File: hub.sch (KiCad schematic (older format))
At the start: 22 parts

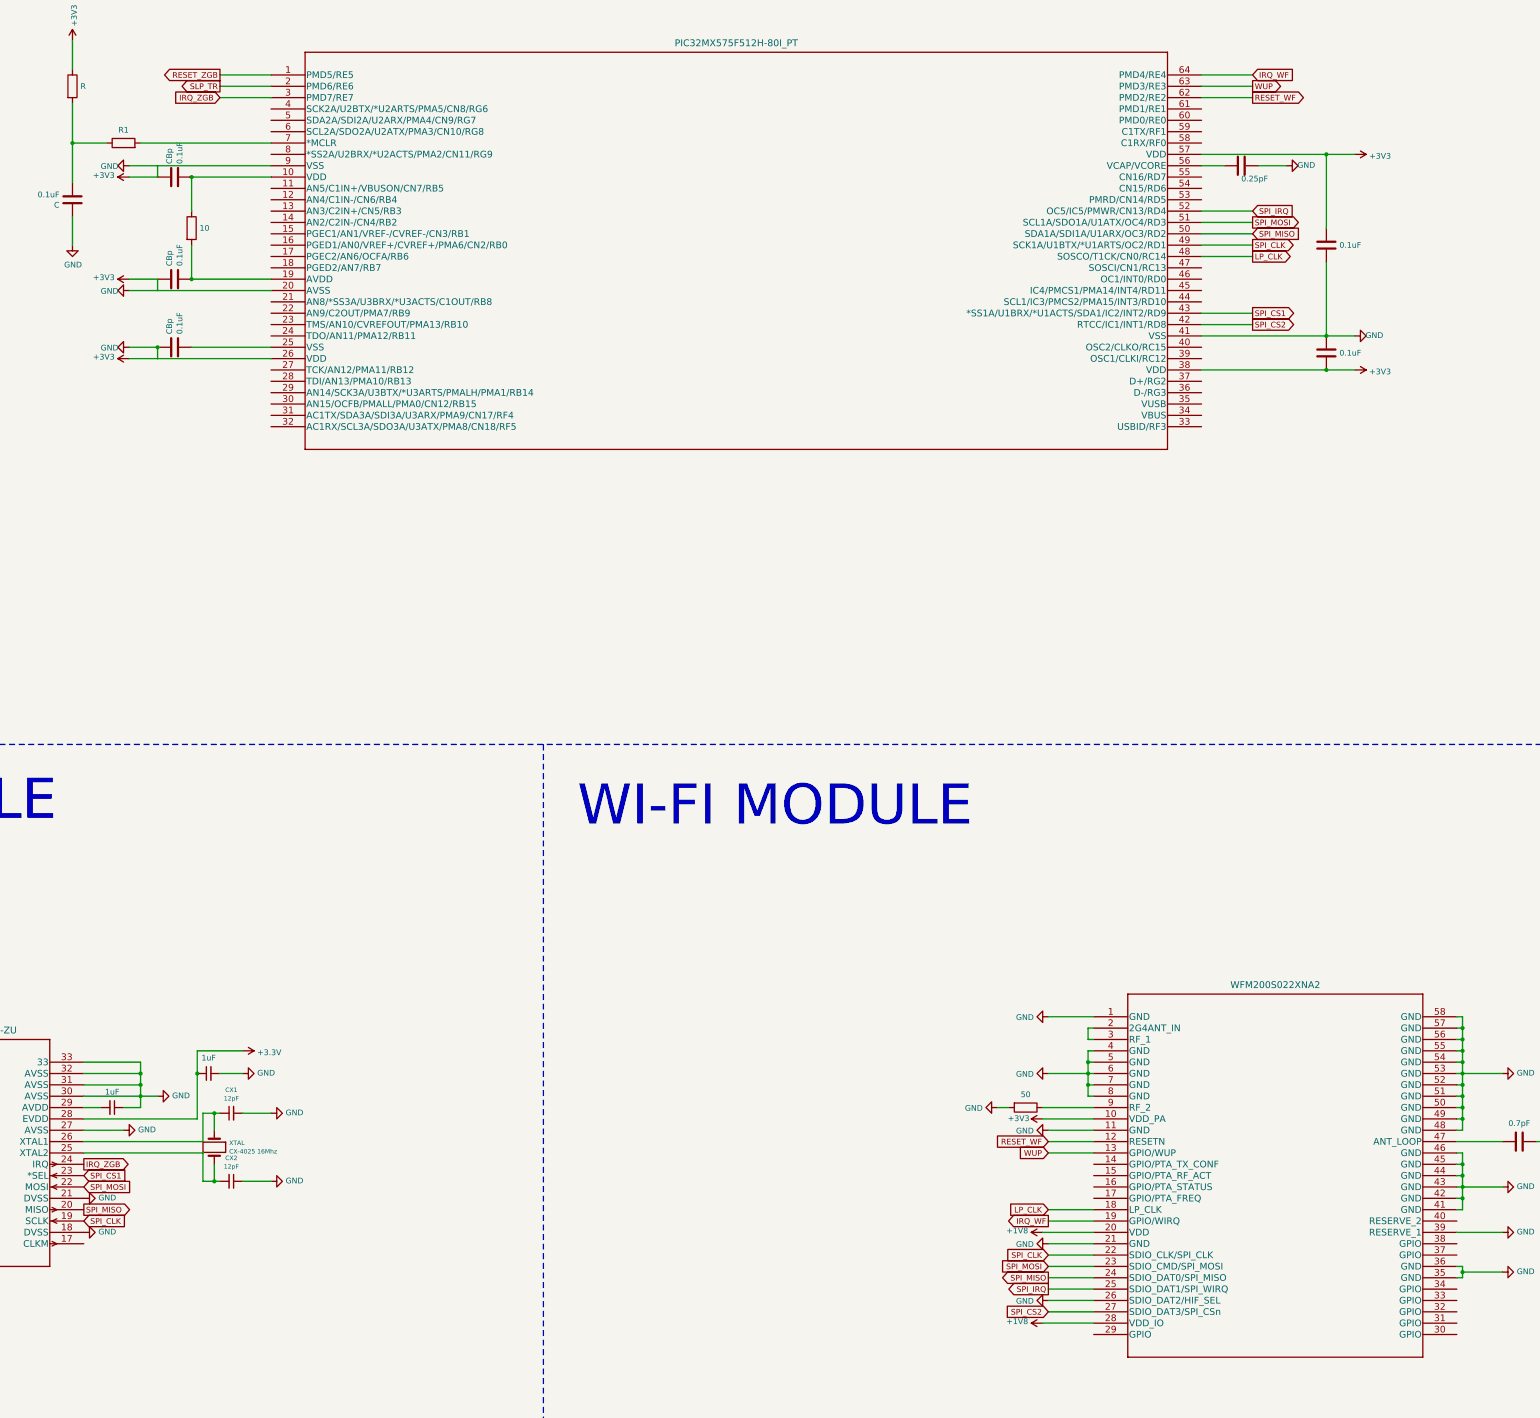
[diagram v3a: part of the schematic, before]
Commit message: Add cube PCB design
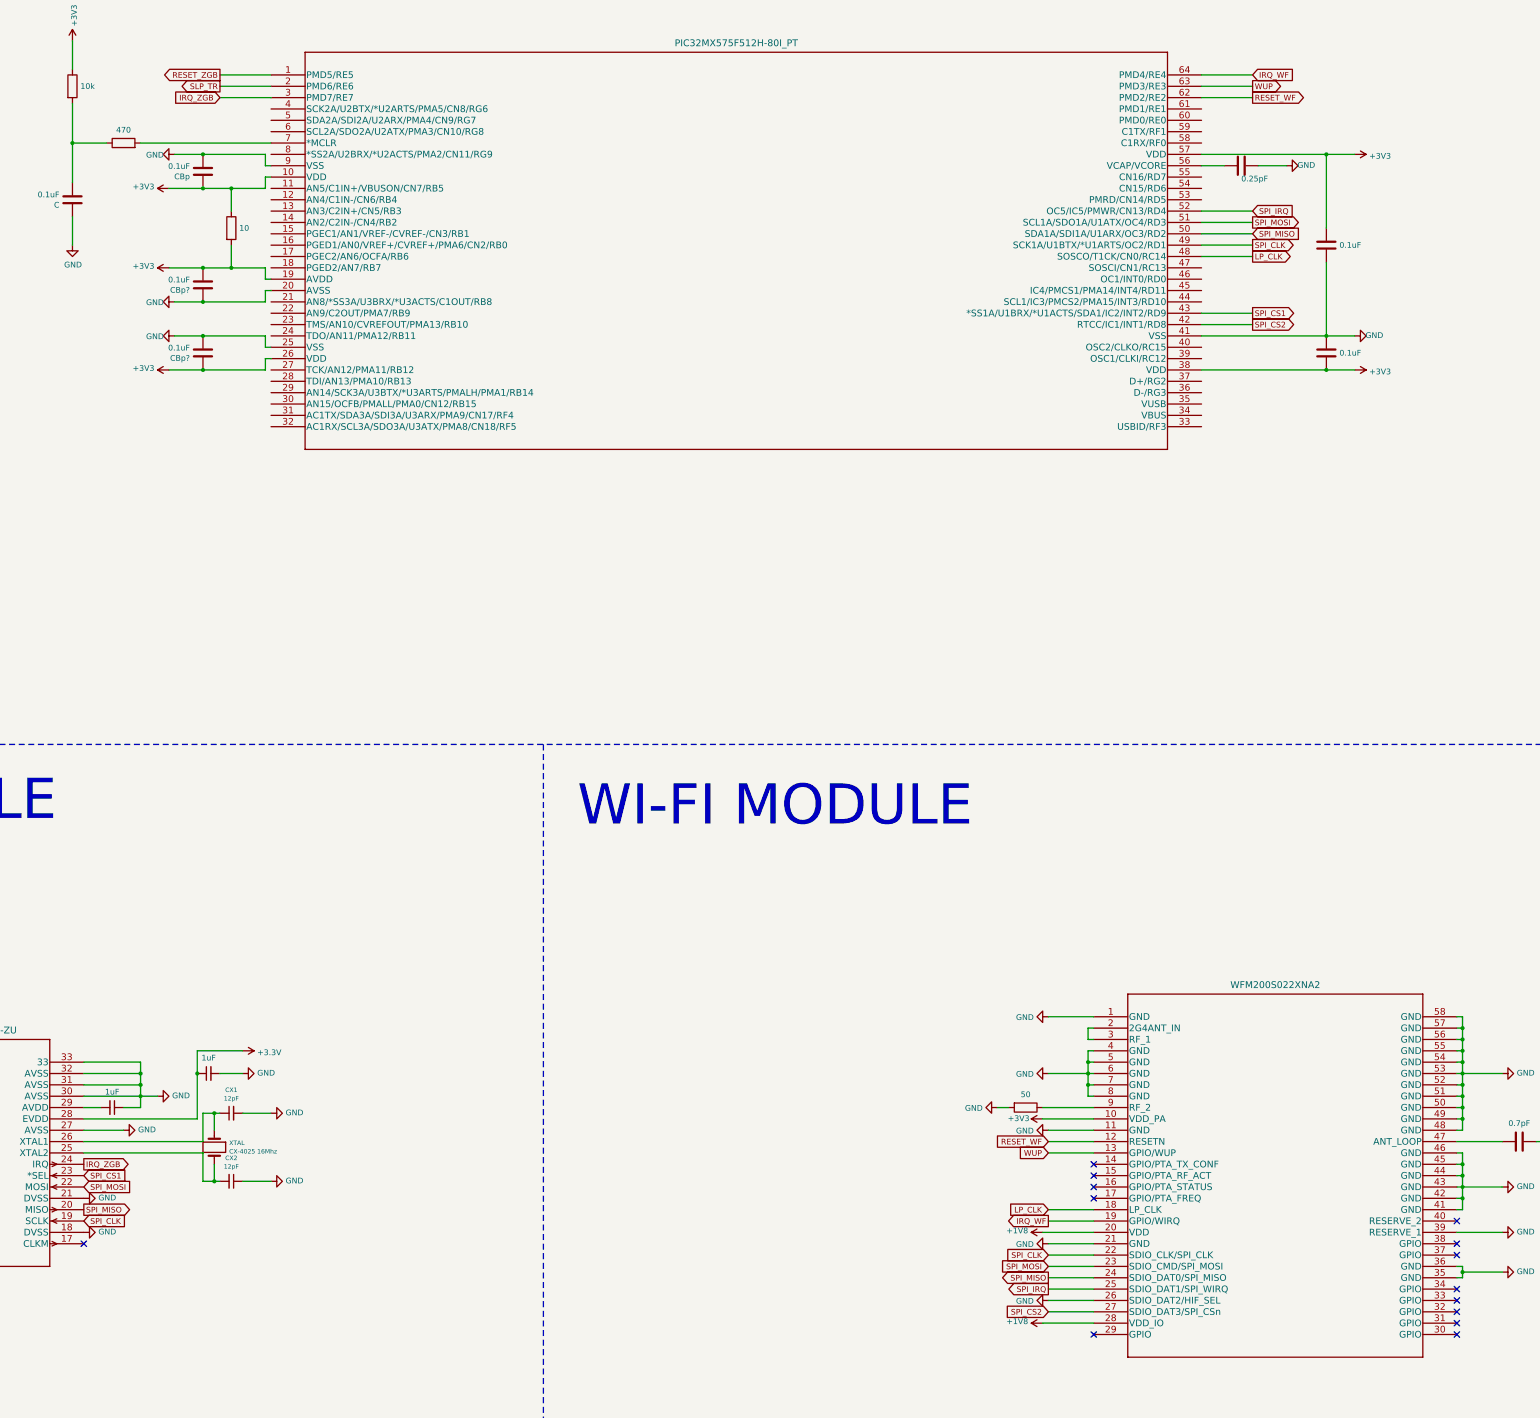
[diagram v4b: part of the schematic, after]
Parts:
- removed CBp (x2): 0.1uF, symbol Device:C
- removed R?: 10, symbol Device:R
- added CBp? (x2): 0.1uF, symbol Device:C
- added r: 10, symbol Device:R
- R?: value R -> 10k
- R?: value R1 -> 470
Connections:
- net +3V3: now also U?.10 (VDD), U?.19 (AVDD), CBp?.1, CBp?.2, r.1, r.2; no longer C.1, C?.1, C?.1, C?.1, C?.2, CB?.1, CB?.2, CB?.2, CX1.2, CX2.1, R?.2, U?.1 (DIG3), U?.10 (DIG2), U?.12 (DVSS), U?.16 (DVSS), U?.18 (DVSS), U?.2 (DIG4), U?.20 (AVSS), U?.21 (DVSS), U?.27 (AVSS), U?.3 (AVSS), U?.30 (AVSS), U?.31 (AVSS), U?.32 (AVSS), U?.33, U?.41 (VSS), U?.6 (AVSS), U?.7 (DVSS), U?.9 (DIG1), U?.9 (VSS), WiFi.1 (GND), WiFi.11 (GND), WiFi.21 (GND), WiFi.26 (SDIO_DAT2/HIF_SEL), WiFi.35 (GND), WiFi.36 (GND), WiFi.39 (RESERVE_1), WiFi.4 (GND), WiFi.41 (GND), WiFi.42 (GND), WiFi.43 (GND), WiFi.44 (GND), WiFi.45 (GND), WiFi.46 (GND), WiFi.48 (GND), WiFi.49 (GND), WiFi.5 (GND), WiFi.50 (GND), WiFi.51 (GND), WiFi.52 (GND), WiFi.53 (GND), WiFi.54 (GND), WiFi.55 (GND), WiFi.56 (GND), WiFi.57 (GND), WiFi.58 (GND), WiFi.6 (GND), WiFi.7 (GND), WiFi.8 (GND), cb.2
- net GND: now reaches CBp.2
- net GND: now also C.1, C?.1, C?.1, C?.1, C?.2, CB?.1, CB?.2, CB?.2, CX1.2, CX2.1, R?.2, U?.1 (DIG3), U?.10 (DIG2), U?.12 (DVSS), U?.16 (DVSS), U?.18 (DVSS), U?.2 (DIG4), U?.20 (AVSS), U?.21 (DVSS), U?.25 (VSS), U?.27 (AVSS), U?.3 (AVSS), U?.30 (AVSS), U?.31 (AVSS), U?.32 (AVSS), U?.33, U?.41 (VSS), U?.6 (AVSS), U?.7 (DVSS), U?.9 (DIG1), U?.9 (VSS), WiFi.1 (GND), WiFi.11 (GND), WiFi.21 (GND), WiFi.26 (SDIO_DAT2/HIF_SEL), WiFi.35 (GND), WiFi.36 (GND), WiFi.39 (RESERVE_1), WiFi.4 (GND), WiFi.41 (GND), WiFi.42 (GND), WiFi.43 (GND), WiFi.44 (GND), WiFi.45 (GND), WiFi.46 (GND), WiFi.48 (GND), WiFi.49 (GND), WiFi.5 (GND), WiFi.50 (GND), WiFi.51 (GND), WiFi.52 (GND), WiFi.53 (GND), WiFi.54 (GND), WiFi.55 (GND), WiFi.56 (GND), WiFi.57 (GND), WiFi.58 (GND), WiFi.6 (GND), WiFi.7 (GND), WiFi.8 (GND), cb.2, CBp?.1, CBp?.2; no longer U?.10 (VDD)
- no-connect marks 0 -> 14
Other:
- moved on the sheet: CBp
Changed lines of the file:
@@
 L Device:C CBp
 U 1 1 609B9B76
-P 5850 3850
-F 0 "CBp" H 5965 3896 50  0000 L CNN
-F 1 "0.1uF" H 5965 3805 50  0000 L CNN
-F 2 "" H 5888 3700 50  0001 C CNN
-F 3 "~" H 5850 3850 50  0001 C CNN
-	1    5850 3850
-	0    -1   -1   0
+P 6100 3800
+F 0 "CBp" H 6215 3846 50  0000 L CNN
+F 1 "0.1uF" H 6215 3755 50  0000 L CNN
+F 2 "" H 6138 3650 50  0001 C CNN
+F 3 "~" H 6100 3800 50  0001 C CNN
+	1    6100 3800
+	-1   0    0    1
 $EndComp
 $Comp
@@
 Wire Wire Line
 	14900 5550 16000 5550
-Wire Wire Line
-	5700 3750 5700 3850
-Wire Wire Line
-	6700 5350 6000 5350
-$Comp
-L Device:C CBp
-U 1 1 60AF944E
-P 5850 5350
-F 0 "CBp" H 5965 5396 50  0000 L CNN
-F 1 "0.1uF" H 5965 5305 50  0000 L CNN
-F 2 "" H 5888 5200 50  0001 C CNN
-F 3 "~" H 5850 5350 50  0001 C CNN
-	1    5850 5350
-	0    -1   -1   0
-$EndComp
-Wire Wire Line
-	5700 5350 5700 5450
-Wire Wire Line
-	5700 5450 6700 5450
-Wire Wire Line
-	6700 4750 6000 4750
-$Comp
-L Device:C CBp
-U 1 1 60B009EA
-P 5850 4750
-F 0 "CBp" H 5965 4796 50  0000 L CNN
-F 1 "0.1uF" H 5965 4705 50  0000 L CNN
-F 2 "" H 5888 4600 50  0001 C CNN
-F 3 "~" H 5850 4750 50  0001 C CNN
-	1    5850 4750
-	0    -1   -1   0
-$EndComp
-Wire Wire Line
-	5700 4750 5700 4850
-Wire Wire Line
-	5700 4850 6700 4850
-Wire Wire Line
-	6000 3850 6700 3850
-Wire Wire Line
-	5700 3750 6700 3750
-Wire Wire Line
-	6000 3850 6000 4150
-Connection ~ 6000 3850
-Connection ~ 6000 4750
-$Comp
-L Device:R R?
-U 1 1 60B1E6B4
-P 6000 4300
-F 0 "R?" H 6070 4346 50  0001 L CNN
-F 1 "10" H 6070 4300 50  0000 L CNN
-F 2 "" V 5930 4300 50  0001 C CNN
-F 3 "~" H 6000 4300 50  0001 C CNN
-	1    6000 4300
-	1    0    0    -1
-$EndComp
-Wire Wire Line
-	6000 4450 6000 4750
 $Comp
 L Device:R R?
@@
 P 4950 3050
 F 0 "R?" H 5020 3096 50  0001 L CNN
-F 1 "R" H 5020 3050 50  0000 L CNN
+F 1 "10k" H 5020 3050 50  0000 L CNN
 F 2 "" V 4880 3050 50  0001 C CNN
 F 3 "~" H 4950 3050 50  0001 C CNN
@@
 $Comp
 L power:GND #PWR?
-U 1 1 60B64186
-P 5450 5350
-F 0 "#PWR?" H 5450 5100 50  0001 C CNN
-F 1 "GND" V 5455 5177 50  0000 C CNN
-F 2 "" H 5450 5350 50  0001 C CNN
-F 3 "" H 5450 5350 50  0001 C CNN
-	1    5450 5350
-	0    1    1    0
-$EndComp
-Wire Wire Line
-	5700 5350 5450 5350
-Connection ~ 5700 5350
-$Comp
-L power:GND #PWR?
-U 1 1 60B8E7D4
-P 5450 4850
-F 0 "#PWR?" H 5450 4600 50  0001 C CNN
-F 1 "GND" V 5455 4677 50  0000 C CNN
-F 2 "" H 5450 4850 50  0001 C CNN
-F 3 "" H 5450 4850 50  0001 C CNN
-	1    5450 4850
-	0    1    1    0
-$EndComp
-Wire Wire Line
-	5700 4850 5450 4850
-$Comp
-L power:GND #PWR?
 U 1 1 60B968B7
-P 5450 3750
-F 0 "#PWR?" H 5450 3500 50  0001 C CNN
-F 1 "GND" V 5455 3577 50  0000 C CNN
-F 2 "" H 5450 3750 50  0001 C CNN
-F 3 "" H 5450 3750 50  0001 C CNN
-	1    5450 3750
-	0    1    1    0
-$EndComp
-Wire Wire Line
-	5700 3750 5450 3750
+P 5850 3650
+F 0 "#PWR?" H 5850 3400 50  0001 C CNN
+F 1 "GND" V 5855 3477 50  0000 C CNN
+F 2 "" H 5850 3650 50  0001 C CNN
+F 3 "" H 5850 3650 50  0001 C CNN
+	1    5850 3650
+	0    1    1    0
+$EndComp
+Wire Wire Line
+	6100 3650 5850 3650
 $Comp
 L power:GND #PWR?
@@
 L power:+3V3 #PWR?
 U 1 1 60BBA40E
-P 5450 3850
-F 0 "#PWR?" H 5450 3700 50  0001 C CNN
-F 1 "+3V3" V 5465 3978 50  0000 L CNN
-F 2 "" H 5450 3850 50  0001 C CNN
-F 3 "" H 5450 3850 50  0001 C CNN
-	1    5450 3850
-	0    -1   -1   0
-$EndComp
-Wire Wire Line
-	5450 3850 5700 3850
-$Comp
-L power:+3V3 #PWR?
-U 1 1 60BC3972
-P 5450 4750
-F 0 "#PWR?" H 5450 4600 50  0001 C CNN
-F 1 "+3V3" V 5465 4878 50  0000 L CNN
-F 2 "" H 5450 4750 50  0001 C CNN
-F 3 "" H 5450 4750 50  0001 C CNN
-	1    5450 4750
-	0    -1   -1   0
-$EndComp
-Wire Wire Line
-	5450 4750 5700 4750
-$Comp
-L power:+3V3 #PWR?
-U 1 1 60BCCAE0
-P 5450 5450
-F 0 "#PWR?" H 5450 5300 50  0001 C CNN
-F 1 "+3V3" V 5465 5578 50  0000 L CNN
-F 2 "" H 5450 5450 50  0001 C CNN
-F 3 "" H 5450 5450 50  0001 C CNN
-	1    5450 5450
-	0    -1   -1   0
-$EndComp
-Wire Wire Line
-	5450 5450 5700 5450
+P 5800 3950
+F 0 "#PWR?" H 5800 3800 50  0001 C CNN
+F 1 "+3V3" V 5815 4078 50  0000 L CNN
+F 2 "" H 5800 3950 50  0001 C CNN
+F 3 "" H 5800 3950 50  0001 C CNN
+	1    5800 3950
+	0    -1   -1   0
+$EndComp
 $Comp
 L Device:R R?
@@
 P 5400 3550
 F 0 "R?" H 5470 3596 50  0001 L CNN
-F 1 "R1" V 5515 3550 50  0000 C CNN
+F 1 "470" V 5515 3550 50  0000 C CNN
 F 2 "" V 5330 3550 50  0001 C CNN
 F 3 "~" H 5400 3550 50  0001 C CNN
@@
 Wire Wire Line
 	14900 4550 15350 4550
+NoConn ~ 13950 12550
+NoConn ~ 13950 12650
+NoConn ~ 13950 12750
+NoConn ~ 13950 12850
+NoConn ~ 13950 14050
+NoConn ~ 17150 14050
+NoConn ~ 17150 13950
+NoConn ~ 17150 13850
+NoConn ~ 17150 13750
+NoConn ~ 17150 13650
+NoConn ~ 17150 13350
+NoConn ~ 17150 13250
+NoConn ~ 17150 13050
+NoConn ~ 5050 13250
+Wire Wire Line
+	6700 3750 6650 3750
+Wire Wire Line
+	6650 3750 6650 3650
+Wire Wire Line
+	6650 3650 6100 3650
+Wire Wire Line
+	6700 3850 6650 3850
+Wire Wire Line
+	6650 3850 6650 3950
+Wire Wire Line
+	6650 3950 6350 3950
+Connection ~ 6100 3650
+Wire Wire Line
+	5800 3950 6100 3950
+Connection ~ 6100 3950
+$Comp
+L Device:C CBp?
+U 1 1 60E901ED
+P 6100 4800
+F 0 "CBp?" H 6215 4846 50  0000 L CNN
+F 1 "0.1uF" H 6215 4755 50  0000 L CNN
+F 2 "" H 6138 4650 50  0001 C CNN
+F 3 "~" H 6100 4800 50  0001 C CNN
+	1    6100 4800
+	-1   0    0    1
+$EndComp
+$Comp
+L power:GND #PWR?
+U 1 1 60E901F3
+P 5850 4950
+F 0 "#PWR?" H 5850 4700 50  0001 C CNN
+F 1 "GND" V 5855 4777 50  0000 C CNN
+F 2 "" H 5850 4950 50  0001 C CNN
+F 3 "" H 5850 4950 50  0001 C CNN
+	1    5850 4950
+	0    1    1    0
+$EndComp
+Wire Wire Line
+	6100 4950 5850 4950
+$Comp
+L power:+3V3 #PWR?
+U 1 1 60E901FA
+P 5800 4650
+F 0 "#PWR?" H 5800 4500 50  0001 C CNN
+F 1 "+3V3" V 5815 4778 50  0000 L CNN
+F 2 "" H 5800 4650 50  0001 C CNN
+F 3 "" H 5800 4650 50  0001 C CNN
+	1    5800 4650
+	0    -1   -1   0
+$EndComp
+Wire Wire Line
+	6700 4750 6650 4750
+Wire Wire Line
+	6650 4750 6650 4650
+Wire Wire Line
+	6650 4650 6350 4650
+Wire Wire Line
+	6700 4850 6650 4850
+Wire Wire Line
+	6650 4850 6650 4950
+Wire Wire Line
+	6650 4950 6100 4950
+Wire Wire Line
+	5800 4650 6100 4650
+$Comp
+L Device:C CBp?
+U 1 1 60E9B904
+P 6100 5400
+F 0 "CBp?" H 6215 5446 50  0000 L CNN
+F 1 "0.1uF" H 6215 5355 50  0000 L CNN
+F 2 "" H 6138 5250 50  0001 C CNN
+F 3 "~" H 6100 5400 50  0001 C CNN
+	1    6100 5400
+	-1   0    0    1
+$EndComp
+$Comp
+L power:GND #PWR?
+U 1 1 60E9B90A
+P 5850 5250
+F 0 "#PWR?" H 5850 5000 50  0001 C CNN
+F 1 "GND" V 5855 5077 50  0000 C CNN
+F 2 "" H 5850 5250 50  0001 C CNN
+F 3 "" H 5850 5250 50  0001 C CNN
+	1    5850 5250
+	0    1    1    0
+$EndComp
+Wire Wire Line
+	6100 5250 5850 5250
+$Comp
+L power:+3V3 #PWR?
+U 1 1 60E9B911
+P 5800 5550
+F 0 "#PWR?" H 5800 5400 50  0001 C CNN
+F 1 "+3V3" V 5815 5678 50  0000 L CNN
+F 2 "" H 5800 5550 50  0001 C CNN
+F 3 "" H 5800 5550 50  0001 C CNN
+	1    5800 5550
+	0    -1   -1   0
+$EndComp
+Wire Wire Line
+	6700 5350 6650 5350
+Wire Wire Line
+	6650 5350 6650 5250
+Wire Wire Line
+	6650 5250 6100 5250
+Wire Wire Line
+	6700 5450 6650 5450
+Wire Wire Line
+	6650 5450 6650 5550
+Wire Wire Line
+	6650 5550 6100 5550
+Connection ~ 6100 5250
+Wire Wire Line
+	5800 5550 6100 5550
+Connection ~ 6100 5550
+Wire Wire Line
+	6350 3950 6350 4150
+Connection ~ 6350 3950
+Wire Wire Line
+	6350 3950 6100 3950
+Connection ~ 6350 4650
+Wire Wire Line
+	6350 4650 6100 4650
+$Comp
+L Device:R r
+U 1 1 60EB346D
+P 6350 4300
+F 0 "r" H 6420 4346 50  0001 L CNN
+F 1 "10" H 6420 4300 50  0000 L CNN
+F 2 "" V 6280 4300 50  0001 C CNN
+F 3 "~" H 6350 4300 50  0001 C CNN
+	1    6350 4300
+	1    0    0    -1
+$EndComp
+Wire Wire Line
+	6350 4450 6350 4650
+Connection ~ 6100 4650
+Connection ~ 6100 4950
 $EndSCHEMATC
